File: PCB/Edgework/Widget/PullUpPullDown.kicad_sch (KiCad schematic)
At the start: 10 parts, among them Q1 Q_PMOS_GSD, Q2 Q_NMOS_GSD

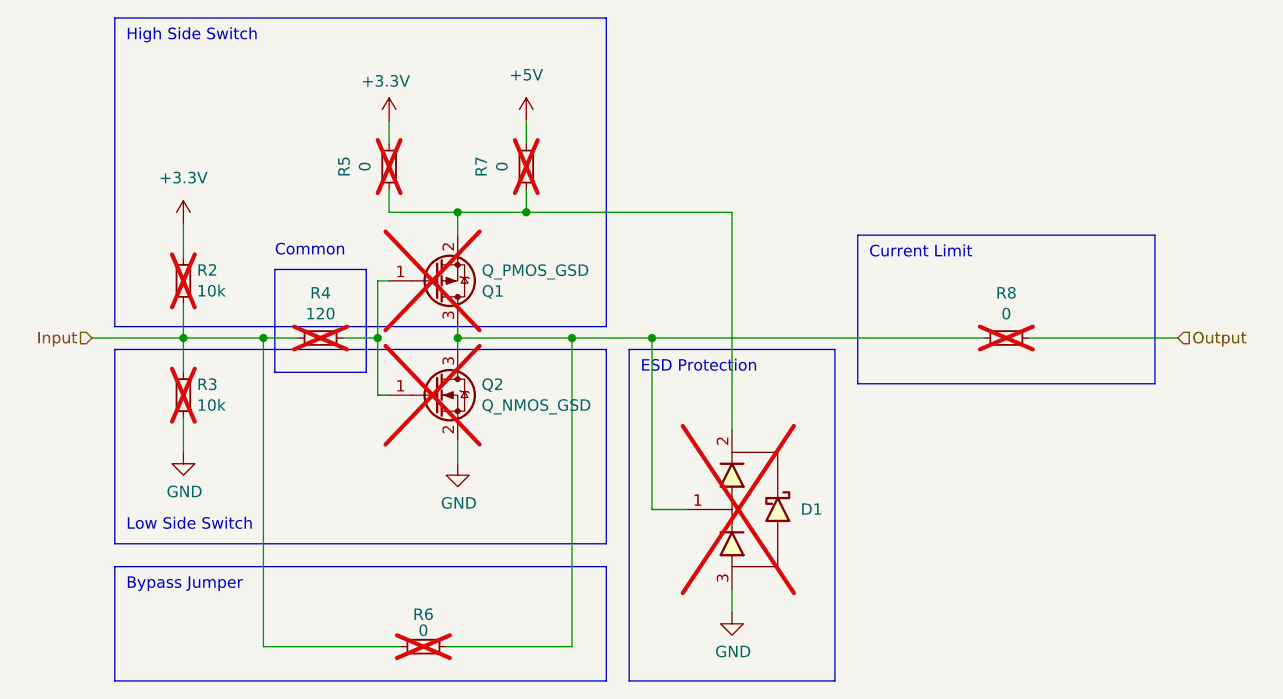
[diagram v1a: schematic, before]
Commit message: feat: Migrate edgework to a STM32G070KBT6.
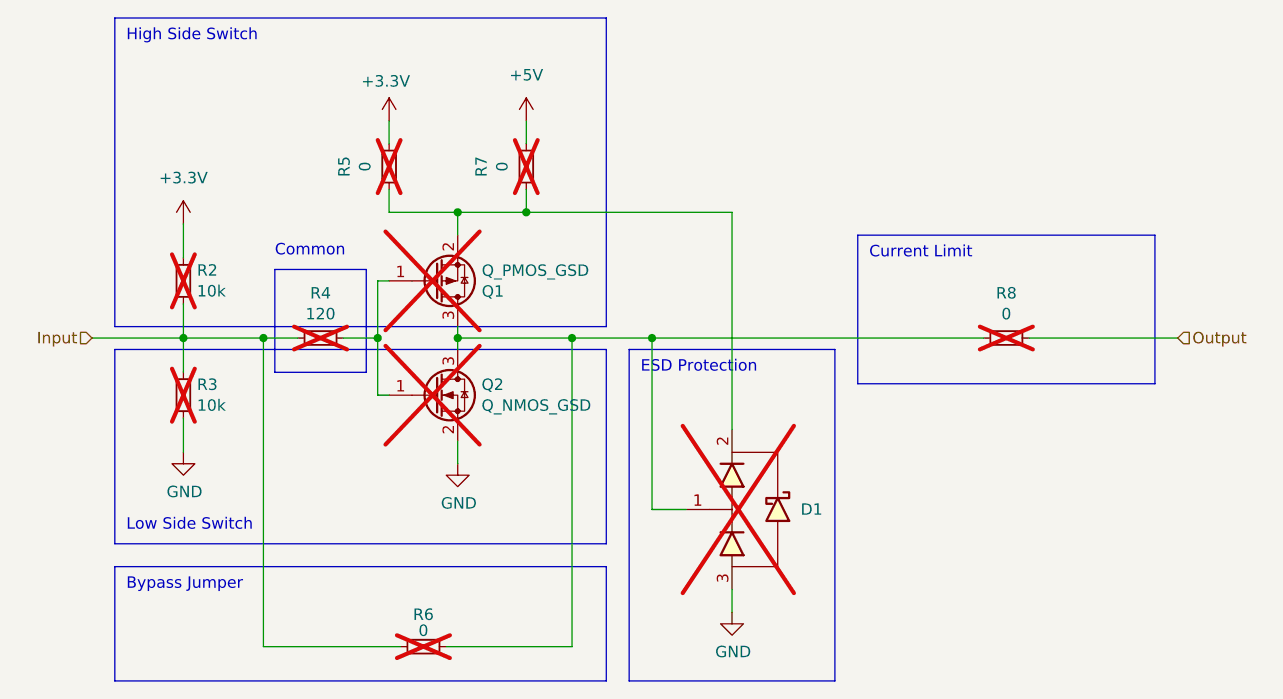
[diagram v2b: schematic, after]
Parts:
- Q1: symbol Device:Q_PMOS_GSD -> Transistor_FET:Q_PMOS_GSD
- Q2: symbol Device:Q_NMOS_GSD -> Transistor_FET:Q_NMOS_GSD
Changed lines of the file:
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@@
 	)
 	(symbol
-		(lib_id "Device:Q_PMOS_GSD")
+		(lib_id "Transistor_FET:Q_PMOS_GSD")
 		(at 59.69 45.72 0)
 		(mirror x)
@@
 			)
 		)
-		(property "Description" ""
+		(property "Description" "P-MOSFET transistor, gate/source/drain"
 			(at 59.69 45.72 0)
 			(hide yes)
@@
 	)
 	(symbol
-		(lib_id "Device:Q_NMOS_GSD")
+		(lib_id "Transistor_FET:Q_NMOS_GSD")
 		(at 59.69 58.42 0)
 		(unit 1)
@@
 			)
 		)
-		(property "Description" ""
+		(property "Description" "N-MOSFET transistor, gate/source/drain"
 			(at 59.69 58.42 0)
 			(hide yes)
